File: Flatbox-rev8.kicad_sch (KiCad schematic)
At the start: 71 parts, among them SW1 SW_Push, SW10 GPIO18, SW11 GPIO25, SW12 GPIO27, SW13 GPIO29, SW14 GPIO19, SW15 GPIO24, SW16 GPIO26, SW17 GPIO28, SW18 GPIO16, SW19 SW_Push, SW2 SW_Push, SW20 SW_Push, SW3 SW_Push, SW4 SW_Push, SW5 SW_Push, SW6 SW_Push, SW7 GPIO9, SW8 GPIO10, SW9 GPIO11, U1 RP2350_60QFN, U2 TLV73333PDBV, U3 W25Q128JVS, Y1 ABM8-272-T3

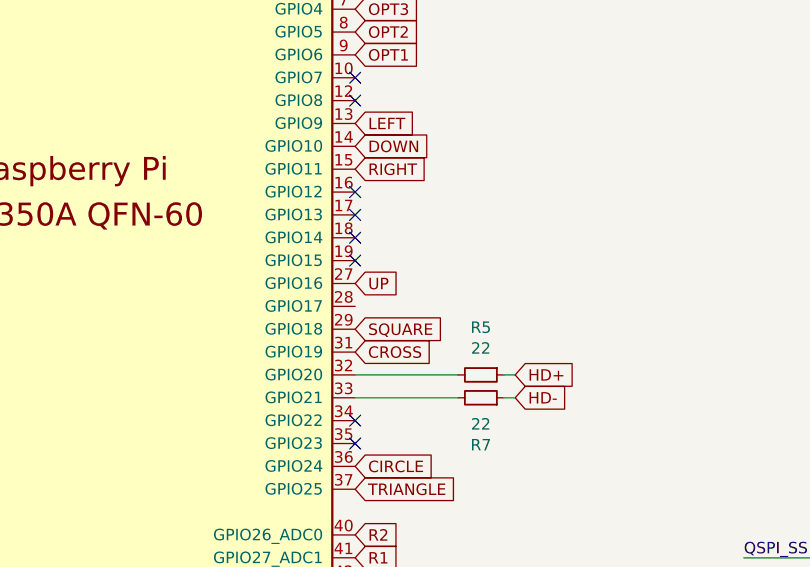
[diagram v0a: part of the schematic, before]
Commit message: Added pinout for case rgb and switch RGB, moved USB to suitable location
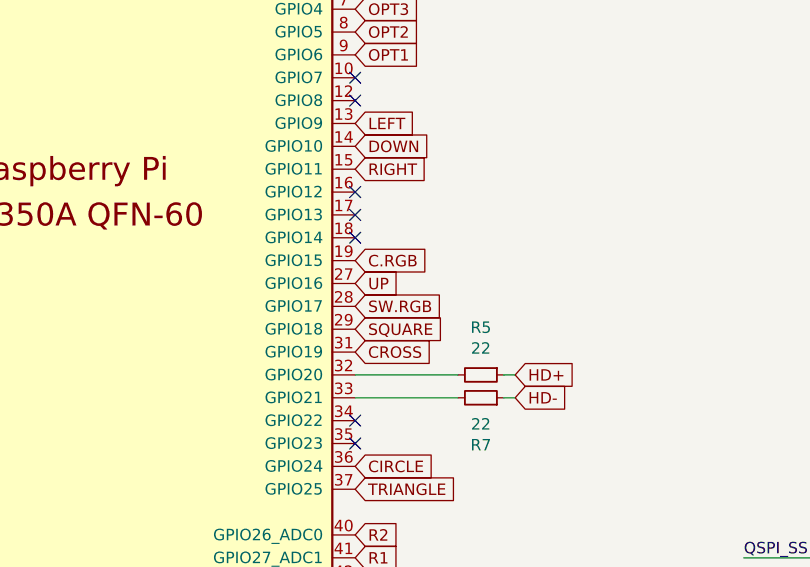
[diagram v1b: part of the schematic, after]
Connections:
- net C.RGB: now reaches U1.19 (GPIO15)
- net SW.RGB: now reaches U1.28 (GPIO17)
- no-connect marks 12 -> 11
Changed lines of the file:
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@@
-	)
-	(no_connect
-		(at 269.24 128.27)
 	)
 	(no_connect
@@
 		)
 	)
+	(global_label "C.RGB"
+		(shape input)
+		(at 269.24 128.27 0)
+		(fields_autoplaced yes)
+		(effects
+			(font
+				(size 1.27 1.27)
+			)
+			(justify left)
+		)
+		(property "Intersheetrefs" "${INTERSHEET_REFS}"
+			(at 277.2558 128.27 0)
+			(effects
+				(font
+					(size 1.27 1.27)
+				)
+				(justify left)
+				(hide yes)
+			)
+		)
+	)
 	(global_label "OPT3"
 		(shape input)
@@
 				(hide yes)
 			)
+		)
+	)
+	(global_label "SW.RGB"
+		(shape input)
+		(at 269.24 133.35 0)
+		(fields_autoplaced yes)
+		(effects
+			(font
+				(size 1.27 1.27)
+			)
+			(justify left)
+		)
+		(property "Intersheetrefs" "${INTERSHEET_REFS}"
+			(at 278.6467 133.35 0)
+			(effects
+				(font
+					(size 1.27 1.27)
+				)
+				(justify left)
+				(hide yes)
+			)

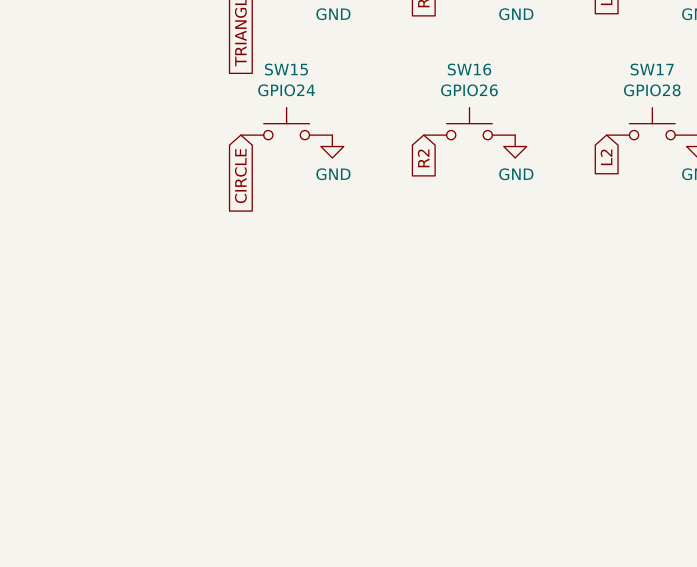
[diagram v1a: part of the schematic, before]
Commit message: Done up switch traces for main directional and command input
Done up switch traces for main directional and command input

Need to redo schematic for LS RS, Up directional chaining and RGB SMD
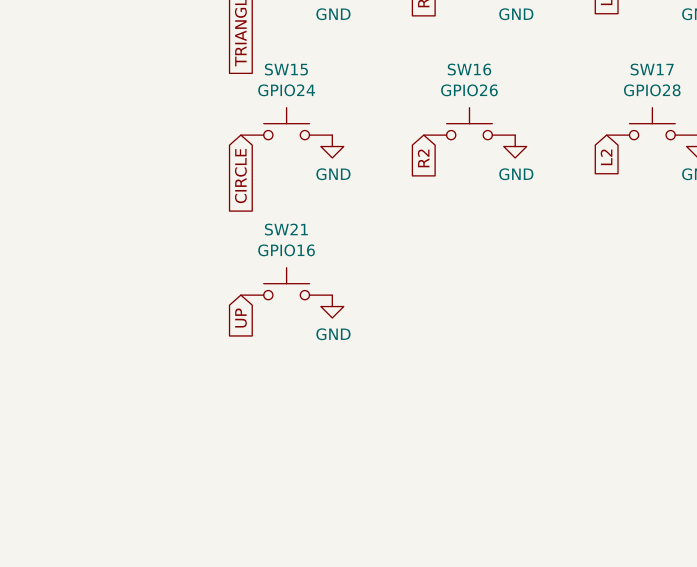
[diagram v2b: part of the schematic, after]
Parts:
- added SW21: GPIO16, Kailh:Kailh_socket_PG1350_optional, symbol Switch:SW_Push
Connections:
- net GND: now also SW21.2
- net UP: now also SW21.1
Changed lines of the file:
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@@
 		)
 	)
+	(global_label "UP"
+		(shape input)
+		(at 41.91 113.03 270)
+		(effects
+			(font
+				(size 1.27 1.27)
+			)
+			(justify right)
+		)
+		(property "Intersheetrefs" "${INTERSHEET_REFS}"
+			(at 41.91 113.03 0)
+			(effects
+				(font
+					(size 1.27 1.27)
+				)
+				(hide yes)
+			)
+		)
+	)
 	(global_label "OPT6"
 		(shape input)
@@
 	)
 	(symbol
+		(lib_id "power:GND")
+		(at 52.07 113.03 0)
+		(unit 1)
+		(exclude_from_sim no)
+		(in_bom yes)
+		(on_board yes)
+		(dnp no)
+		(property "Reference" "#PWR019"
+			(at 52.07 119.38 0)
+			(effects
+				(font
+					(size 1.27 1.27)
+				)
+				(hide yes)
+			)
+		)
+		(property "Value" "GND"
+			(at 52.197 117.4242 0)
+			(effects
+				(font
+					(size 1.27 1.27)
+				)
+			)
+		)
+		(property "Footprint" ""
+			(at 52.07 113.03 0)
+			(effects
+				(font
+					(size 1.27 1.27)
+				)
+				(hide yes)
+			)
+		)
+		(property "Datasheet" ""
+			(at 52.07 113.03 0)
+			(effects
+				(font
+					(size 1.27 1.27)
+				)
+				(hide yes)
+			)
+		)
+		(property "Description" ""
+			(at 52.07 113.03 0)
+			(effects
+				(font
+					(size 1.27 1.27)
+				)
+				(hide yes)
+			)
+		)
+		(pin "1"
+		)
+		(instances
+			(project "Flatbox-rev8"
+				(path "/15f2e5be-6a22-46eb-955b-5555ace1bee2"
+					(reference "#PWR019")
+					(unit 1)
+				)
+			)
+		)
+	)
+	(symbol
 		(lib_id "Mechanical:MountingHole")
 		(at 39.37 257.81 0)
@@
 					(unit 1)
 				)
+			)
+		)
+	)
+	(symbol
+		(lib_id "Switch:SW_Push")
+		(at 46.99 113.03 0)
+		(unit 1)
+		(exclude_from_sim no)
+		(in_bom no)
+		(on_board yes)
+		(dnp no)
+		(property "Reference" "SW21"
+			(at 46.99 105.791 0)
+			(effects
+				(font
+					(size 1.27 1.27)
+				)
+			)
+		)
+		(property "Value" "GPIO16"
+			(at 46.99 108.1024 0)
+			(effects
+				(font
+					(size 1.27 1.27)
+				)
+			)
+		)
+		(property "Footprint" "Kailh:Kailh_socket_PG1350_optional"
+			(at 46.99 107.95 0)
+			(effects
+				(font
+					(size 1.27 1.27)
+				)
+				(hide yes)
+			)
+		)
+		(property "Datasheet" "~"
+			(at 46.99 107.95 0)
+			(effects
+				(font
+					(size 1.27 1.27)
+				)
+				(hide yes)
+			)
+		)
+		(property "Description" ""
+			(at 46.99 113.03 0)
+			(effects
+				(font
+					(size 1.27 1.27)
+				)
+				(hide yes)
+			)
+		)
+		(property "LCSC" ""
+			(at 46.99 113.03 0)
+			(effects
+				(font
+					(size 1.27 1.27)
+				)
+				(hide yes)
+			)
+		)
+		(pin "1"
+		)
+		(pin "2"
+		)
+		(instances
+			(project "Flatbox-rev8"
+				(path "/15f2e5be-6a22-46eb-955b-5555ace1bee2"
+					(reference "SW21")
+					(unit 1)
+				)

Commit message: final design inshallah
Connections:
- net SCL: now reaches U1.16 (GPIO12)
- net SDA: now reaches U1.17 (GPIO13)
- net LS: now reaches U1.18 (GPIO14)
- net C.RGB renamed RS
- no-connect marks 11 -> 8
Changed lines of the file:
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@@
-	)
-	(no_connect
-		(at 269.24 123.19)
 	)
 	(no_connect
@@
 	)
 	(no_connect
-		(at 269.24 125.73)
-	)
-	(no_connect
 		(at 269.24 110.49)
 	)
@@
 	)
 	(no_connect
-		(at 269.24 120.65)
-	)
-	(no_connect
 		(at 110.49 231.14)
 	)
@@
 		)
 	)
-	(global_label "C.RGB"
+	(global_label "RS"
 		(shape input)
 		(at 269.24 128.27 0)
@@
 		)
 		(property "Intersheetrefs" "${INTERSHEET_REFS}"
-			(at 277.2558 128.27 0)
+			(at 274.0505 128.27 0)
 			(effects
 				(font
@@
 		)
 	)
+	(global_label "SDA"
+		(shape input)
+		(at 269.24 123.19 0)
+		(fields_autoplaced yes)
+		(effects
+			(font
+				(size 1.27 1.27)
+			)
+			(justify left)
+		)
+		(property "Intersheetrefs" "${INTERSHEET_REFS}"
+			(at 275.1391 123.19 0)
+			(effects
+				(font
+					(size 1.27 1.27)
+				)
+				(justify left)
+				(hide yes)
+			)
+		)
+	)
 	(global_label "CROSS"
 		(shape input)
@@
 		)
 	)
+	(global_label "LS"
+		(shape input)
+		(at 269.24 125.73 0)
+		(fields_autoplaced yes)
+		(effects
+			(font
+				(size 1.27 1.27)
+			)
+			(justify left)
+		)
+		(property "Intersheetrefs" "${INTERSHEET_REFS}"
+			(at 273.8086 125.73 0)
+			(effects
+				(font
+					(size 1.27 1.27)
+				)
+				(justify left)
+				(hide yes)
+			)
+		)
+	)
 	(global_label "UP"
 		(shape input)
@@
 			(effects
 				(font
+					(size 1.27 1.27)
+				)
+				(justify left)
+				(hide yes)
+			)
+		)
+	)
+	(global_label "SCL"
+		(shape input)
+		(at 269.24 120.65 0)
+		(fields_autoplaced yes)
+		(effects
+			(font
+				(size 1.27 1.27)
+			)
+			(justify left)
+		)
+		(property "Intersheetrefs" "${INTERSHEET_REFS}"
+			(at 275.0786 120.65 0)
+			(effects
+				(font
